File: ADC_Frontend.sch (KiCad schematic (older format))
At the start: 3 parts

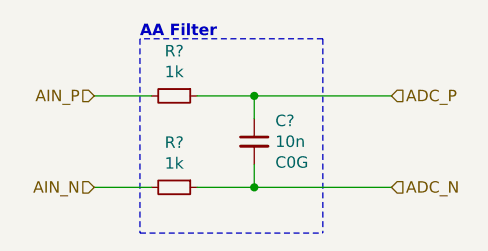
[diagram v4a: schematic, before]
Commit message: Add PWR Flags
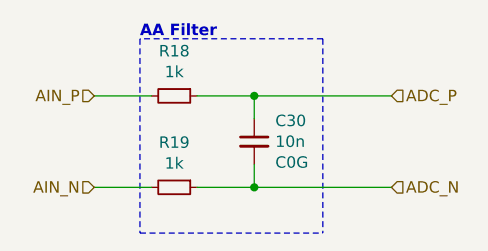
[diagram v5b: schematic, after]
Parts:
- gave numbers to parts that had none: 3
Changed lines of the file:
@@
 AR Path="/5EFC0F96/5EF8AB51" Ref="R?"  Part="1"
 AR Path="/5EFC2E33/5EF8AB51" Ref="R?"  Part="1"
-AR Path="/5EE5ECAD/5EE62BAF/5EF8AB51" Ref="R?"  Part="1"
+AR Path="/5EE5ECAD/5EE62BAF/5EF8AB51" Ref="R12"  Part="1"
 AR Path="/5EE5ECAD/5EE62BB5/5EF8AB51" Ref="R?"  Part="1"
 AR Path="/5EE5ECAD/5EE62BBB/5EF8AB51" Ref="R?"  Part="1"
 AR Path="/5EE5ECAD/5EE62BC1/5EF8AB51" Ref="R?"  Part="1"
-AR Path="/5EE5ECAD/5EE8F492/5EF8AB51" Ref="R?"  Part="1"
-AR Path="/5EE5ECAD/5EE91C90/5EF8AB51" Ref="R?"  Part="1"
-AR Path="/5EE5ECAD/5EE9492B/5EF8AB51" Ref="R?"  Part="1"
-F 0 "R?" V 2854 2450 50  0000 C CNN
+AR Path="/5EE5ECAD/5EE8F492/5EF8AB51" Ref="R14"  Part="1"
+AR Path="/5EE5ECAD/5EE91C90/5EF8AB51" Ref="R16"  Part="1"
+AR Path="/5EE5ECAD/5EE9492B/5EF8AB51" Ref="R18"  Part="1"
+F 0 "R18" V 2854 2450 50  0000 C CNN
 F 1 "1k" V 2945 2450 50  0000 C CNN
 F 2 "" H 3050 2450 50  0001 C CNN
@@
 AR Path="/5EFC0F96/5EF8AB5E" Ref="C?"  Part="1"
 AR Path="/5EFC2E33/5EF8AB5E" Ref="C?"  Part="1"
-AR Path="/5EE5ECAD/5EE62BAF/5EF8AB5E" Ref="C?"  Part="1"
+AR Path="/5EE5ECAD/5EE62BAF/5EF8AB5E" Ref="C27"  Part="1"
 AR Path="/5EE5ECAD/5EE62BB5/5EF8AB5E" Ref="C?"  Part="1"
 AR Path="/5EE5ECAD/5EE62BBB/5EF8AB5E" Ref="C?"  Part="1"
 AR Path="/5EE5ECAD/5EE62BC1/5EF8AB5E" Ref="C?"  Part="1"
-AR Path="/5EE5ECAD/5EE8F492/5EF8AB5E" Ref="C?"  Part="1"
-AR Path="/5EE5ECAD/5EE91C90/5EF8AB5E" Ref="C?"  Part="1"
-AR Path="/5EE5ECAD/5EE9492B/5EF8AB5E" Ref="C?"  Part="1"
-F 0 "C?" H 3492 2741 50  0000 L CNN
+AR Path="/5EE5ECAD/5EE8F492/5EF8AB5E" Ref="C28"  Part="1"
+AR Path="/5EE5ECAD/5EE91C90/5EF8AB5E" Ref="C29"  Part="1"
+AR Path="/5EE5ECAD/5EE9492B/5EF8AB5E" Ref="C30"  Part="1"
+F 0 "C30" H 3492 2741 50  0000 L CNN
 F 1 "10n" H 3492 2650 50  0000 L CNN
 F 2 "" H 3400 2650 50  0001 C CNN
@@
 AR Path="/5EFC0F96/5EF8D41D" Ref="R?"  Part="1"
 AR Path="/5EFC2E33/5EF8D41D" Ref="R?"  Part="1"
-AR Path="/5EE5ECAD/5EE62BAF/5EF8D41D" Ref="R?"  Part="1"
+AR Path="/5EE5ECAD/5EE62BAF/5EF8D41D" Ref="R13"  Part="1"
 AR Path="/5EE5ECAD/5EE62BB5/5EF8D41D" Ref="R?"  Part="1"
 AR Path="/5EE5ECAD/5EE62BBB/5EF8D41D" Ref="R?"  Part="1"
 AR Path="/5EE5ECAD/5EE62BC1/5EF8D41D" Ref="R?"  Part="1"
-AR Path="/5EE5ECAD/5EE8F492/5EF8D41D" Ref="R?"  Part="1"
-AR Path="/5EE5ECAD/5EE91C90/5EF8D41D" Ref="R?"  Part="1"
-AR Path="/5EE5ECAD/5EE9492B/5EF8D41D" Ref="R?"  Part="1"
-F 0 "R?" V 2854 2850 50  0000 C CNN
+AR Path="/5EE5ECAD/5EE8F492/5EF8D41D" Ref="R15"  Part="1"
+AR Path="/5EE5ECAD/5EE91C90/5EF8D41D" Ref="R17"  Part="1"
+AR Path="/5EE5ECAD/5EE9492B/5EF8D41D" Ref="R19"  Part="1"
+F 0 "R19" V 2854 2850 50  0000 C CNN
 F 1 "1k" V 2945 2850 50  0000 C CNN
 F 2 "" H 3050 2850 50  0001 C CNN

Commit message: Assign footprints for all components
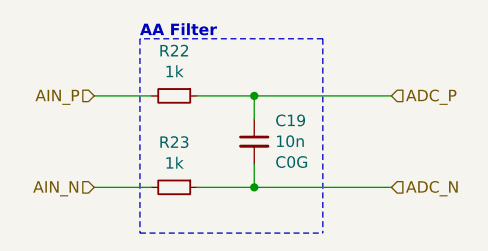
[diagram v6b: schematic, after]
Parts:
- C16: renamed from C27; footprint (none) -> Capacitor_SMD:C_0603_1608Metric_Pad1.05x0.95mm_HandSolder
- R16: renamed from R12; footprint (none) -> Resistor_SMD:R_0603_1608Metric_Pad1.05x0.95mm_HandSolder; MPN (none) -> ERJ-3RBD102V; Mfr. (none) -> Panasonic
- R17: renamed from R13; footprint (none) -> Resistor_SMD:R_0603_1608Metric_Pad1.05x0.95mm_HandSolder
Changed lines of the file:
@@
 $Descr A4 11693 8268
 encoding utf-8
-Sheet 4 15
+Sheet 6 15
 Title "Kleinvoet"
 Date "2020-06-11"
@@
 AR Path="/5EFC0F96/5EF8AB51" Ref="R?"  Part="1"
 AR Path="/5EFC2E33/5EF8AB51" Ref="R?"  Part="1"
-AR Path="/5EE5ECAD/5EE62BAF/5EF8AB51" Ref="R12"  Part="1"
+AR Path="/5EE5ECAD/5EE62BAF/5EF8AB51" Ref="R16"  Part="1"
 AR Path="/5EE5ECAD/5EE62BB5/5EF8AB51" Ref="R?"  Part="1"
 AR Path="/5EE5ECAD/5EE62BBB/5EF8AB51" Ref="R?"  Part="1"
 AR Path="/5EE5ECAD/5EE62BC1/5EF8AB51" Ref="R?"  Part="1"
-AR Path="/5EE5ECAD/5EE8F492/5EF8AB51" Ref="R14"  Part="1"
-AR Path="/5EE5ECAD/5EE91C90/5EF8AB51" Ref="R16"  Part="1"
-AR Path="/5EE5ECAD/5EE9492B/5EF8AB51" Ref="R18"  Part="1"
-F 0 "R18" V 2854 2450 50  0000 C CNN
+AR Path="/5EE5ECAD/5EE8F492/5EF8AB51" Ref="R18"  Part="1"
+AR Path="/5EE5ECAD/5EE91C90/5EF8AB51" Ref="R20"  Part="1"
+AR Path="/5EE5ECAD/5EE9492B/5EF8AB51" Ref="R22"  Part="1"
+F 0 "R22" V 2854 2450 50  0000 C CNN
 F 1 "1k" V 2945 2450 50  0000 C CNN
-F 2 "" H 3050 2450 50  0001 C CNN
+F 2 "Resistor_SMD:R_0603_1608Metric_Pad1.05x0.95mm_HandSolder" H 3050 2450 50  0001 C CNN
 F 3 "~" H 3050 2450 50  0001 C CNN
+F 4 "ERJ-3RBD102V" V 3050 2450 50  0001 C CNN "MPN"
+F 5 "Panasonic" V 3050 2450 50  0001 C CNN "Mfr."
 	1    3050 2450
 	0    1    1    0
@@
 AR Path="/5EFC0F96/5EF8AB5E" Ref="C?"  Part="1"
 AR Path="/5EFC2E33/5EF8AB5E" Ref="C?"  Part="1"
-AR Path="/5EE5ECAD/5EE62BAF/5EF8AB5E" Ref="C27"  Part="1"
+AR Path="/5EE5ECAD/5EE62BAF/5EF8AB5E" Ref="C16"  Part="1"
 AR Path="/5EE5ECAD/5EE62BB5/5EF8AB5E" Ref="C?"  Part="1"
 AR Path="/5EE5ECAD/5EE62BBB/5EF8AB5E" Ref="C?"  Part="1"
 AR Path="/5EE5ECAD/5EE62BC1/5EF8AB5E" Ref="C?"  Part="1"
-AR Path="/5EE5ECAD/5EE8F492/5EF8AB5E" Ref="C28"  Part="1"
-AR Path="/5EE5ECAD/5EE91C90/5EF8AB5E" Ref="C29"  Part="1"
-AR Path="/5EE5ECAD/5EE9492B/5EF8AB5E" Ref="C30"  Part="1"
-F 0 "C30" H 3492 2741 50  0000 L CNN
+AR Path="/5EE5ECAD/5EE8F492/5EF8AB5E" Ref="C17"  Part="1"
+AR Path="/5EE5ECAD/5EE91C90/5EF8AB5E" Ref="C18"  Part="1"
+AR Path="/5EE5ECAD/5EE9492B/5EF8AB5E" Ref="C19"  Part="1"
+F 0 "C19" H 3492 2741 50  0000 L CNN
 F 1 "10n" H 3492 2650 50  0000 L CNN
-F 2 "" H 3400 2650 50  0001 C CNN
+F 2 "Capacitor_SMD:C_0603_1608Metric_Pad1.05x0.95mm_HandSolder" H 3400 2650 50  0001 C CNN
 F 3 "~" H 3400 2650 50  0001 C CNN
 F 4 "C0G" H 3492 2559 50  0000 L CNN "Notes"
@@
 AR Path="/5EFC0F96/5EF8D41D" Ref="R?"  Part="1"
 AR Path="/5EFC2E33/5EF8D41D" Ref="R?"  Part="1"
-AR Path="/5EE5ECAD/5EE62BAF/5EF8D41D" Ref="R13"  Part="1"
+AR Path="/5EE5ECAD/5EE62BAF/5EF8D41D" Ref="R17"  Part="1"
 AR Path="/5EE5ECAD/5EE62BB5/5EF8D41D" Ref="R?"  Part="1"
 AR Path="/5EE5ECAD/5EE62BBB/5EF8D41D" Ref="R?"  Part="1"
 AR Path="/5EE5ECAD/5EE62BC1/5EF8D41D" Ref="R?"  Part="1"
-AR Path="/5EE5ECAD/5EE8F492/5EF8D41D" Ref="R15"  Part="1"
-AR Path="/5EE5ECAD/5EE91C90/5EF8D41D" Ref="R17"  Part="1"
-AR Path="/5EE5ECAD/5EE9492B/5EF8D41D" Ref="R19"  Part="1"
-F 0 "R19" V 2854 2850 50  0000 C CNN
+AR Path="/5EE5ECAD/5EE8F492/5EF8D41D" Ref="R19"  Part="1"
+AR Path="/5EE5ECAD/5EE91C90/5EF8D41D" Ref="R21"  Part="1"
+AR Path="/5EE5ECAD/5EE9492B/5EF8D41D" Ref="R23"  Part="1"
+F 0 "R23" V 2854 2850 50  0000 C CNN
 F 1 "1k" V 2945 2850 50  0000 C CNN
-F 2 "" H 3050 2850 50  0001 C CNN
+F 2 "Resistor_SMD:R_0603_1608Metric_Pad1.05x0.95mm_HandSolder" H 3050 2850 50  0001 C CNN
 F 3 "~" H 3050 2850 50  0001 C CNN
 	1    3050 2850

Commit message: Change Mic Preamp
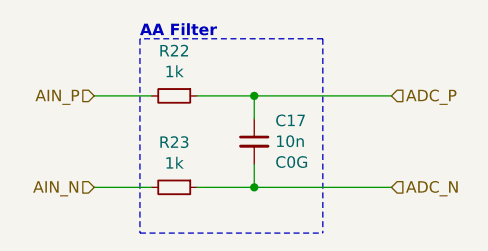
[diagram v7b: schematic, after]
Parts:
- C14: renamed from C16; MPN (none) -> C0603C103J5RACTU; Mfr. (none) -> KEMET
- R17: MPN (none) -> ERJ-3RBD102V; Mfr. (none) -> Panasonic
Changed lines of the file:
@@
 AR Path="/5EFC0F96/5EF8AB5E" Ref="C?"  Part="1"
 AR Path="/5EFC2E33/5EF8AB5E" Ref="C?"  Part="1"
-AR Path="/5EE5ECAD/5EE62BAF/5EF8AB5E" Ref="C16"  Part="1"
+AR Path="/5EE5ECAD/5EE62BAF/5EF8AB5E" Ref="C14"  Part="1"
 AR Path="/5EE5ECAD/5EE62BB5/5EF8AB5E" Ref="C?"  Part="1"
 AR Path="/5EE5ECAD/5EE62BBB/5EF8AB5E" Ref="C?"  Part="1"
 AR Path="/5EE5ECAD/5EE62BC1/5EF8AB5E" Ref="C?"  Part="1"
-AR Path="/5EE5ECAD/5EE8F492/5EF8AB5E" Ref="C17"  Part="1"
-AR Path="/5EE5ECAD/5EE91C90/5EF8AB5E" Ref="C18"  Part="1"
-AR Path="/5EE5ECAD/5EE9492B/5EF8AB5E" Ref="C19"  Part="1"
-F 0 "C19" H 3492 2741 50  0000 L CNN
+AR Path="/5EE5ECAD/5EE8F492/5EF8AB5E" Ref="C15"  Part="1"
+AR Path="/5EE5ECAD/5EE91C90/5EF8AB5E" Ref="C16"  Part="1"
+AR Path="/5EE5ECAD/5EE9492B/5EF8AB5E" Ref="C17"  Part="1"
+F 0 "C17" H 3492 2741 50  0000 L CNN
 F 1 "10n" H 3492 2650 50  0000 L CNN
 F 2 "Capacitor_SMD:C_0603_1608Metric_Pad1.05x0.95mm_HandSolder" H 3400 2650 50  0001 C CNN
 F 3 "~" H 3400 2650 50  0001 C CNN
 F 4 "C0G" H 3492 2559 50  0000 L CNN "Notes"
+F 5 "C0603C103J5RACTU" H 3400 2650 50  0001 C CNN "MPN"
+F 6 "KEMET" H 3400 2650 50  0001 C CNN "Mfr."
 	1    3400 2650
 	1    0    0    -1
@@
 F 2 "Resistor_SMD:R_0603_1608Metric_Pad1.05x0.95mm_HandSolder" H 3050 2850 50  0001 C CNN
 F 3 "~" H 3050 2850 50  0001 C CNN
+F 4 "ERJ-3RBD102V" H 3050 2850 50  0001 C CNN "MPN"
+F 5 "Panasonic" H 3050 2850 50  0001 C CNN "Mfr."
 	1    3050 2850
 	0    1    1    0
